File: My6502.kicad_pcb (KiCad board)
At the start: 2 copper layers, 99.7 x 99.7 mm, 28 parts, among them J1 IRQ_SEL, J2 CLK Jumper, J4 Expansion Port, J5 IRQ_Pullup, SW1 RESET, U1 ROM 28C256, U2 CPU 6502, U3 RAM 62256, U4 74HCT00, U5 74HCT02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

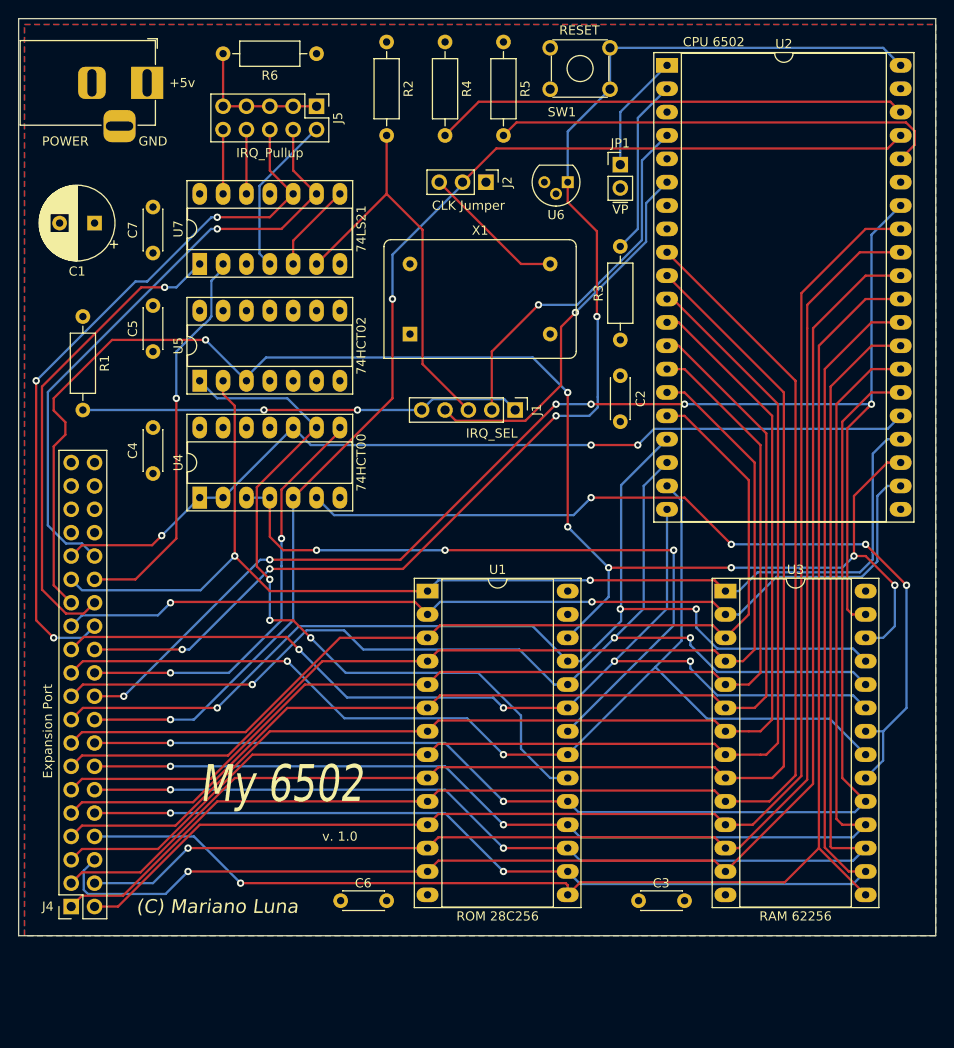
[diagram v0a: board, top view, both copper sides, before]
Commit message: Edge board completed and routed
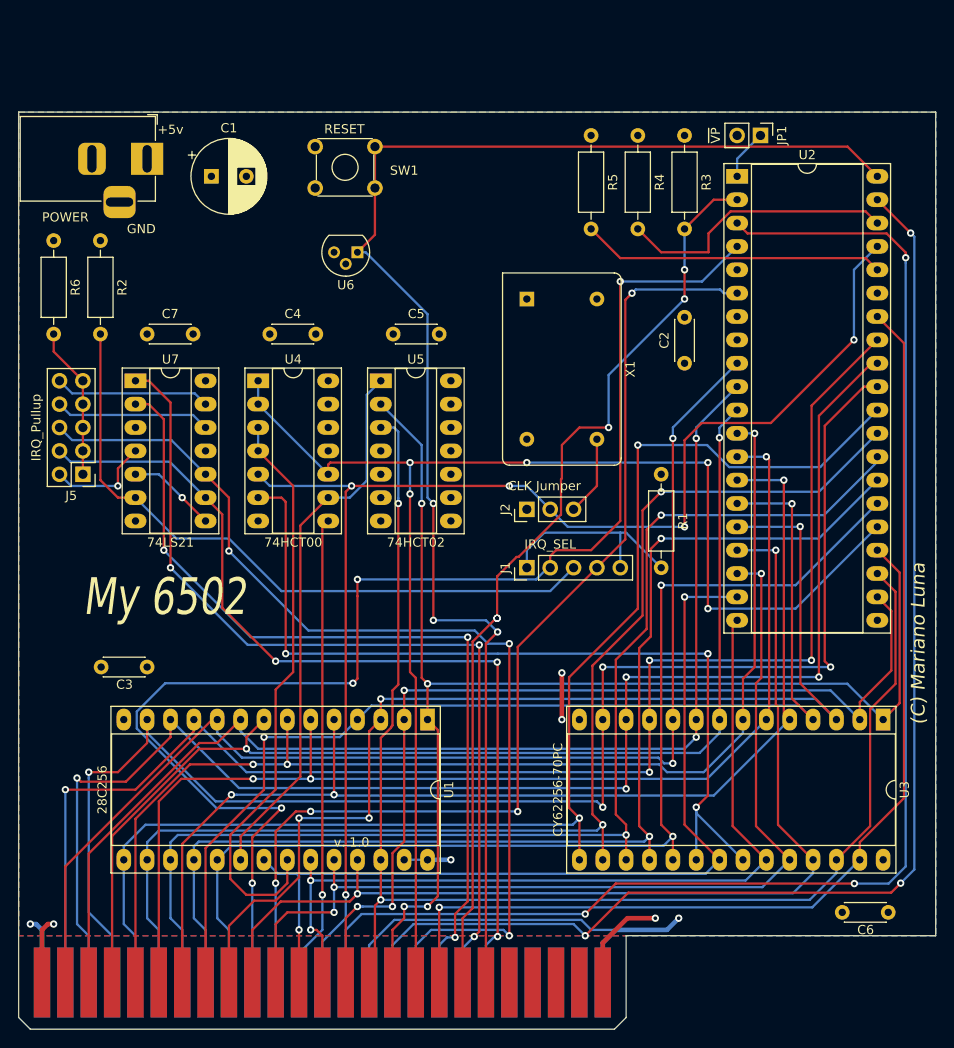
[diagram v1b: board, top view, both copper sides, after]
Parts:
- removed J4: Expansion Port, Connector_PinSocket_2.54mm:PinSocket_2x20_P2.54mm_Vertical
- added 6502_BUS1: 6502_BUS, A2_Slot_Footorint:BUS_A2, F.Cu at (56.5, 154.9)
- U1: value ROM 28C256 -> 28C256
- U2: value CPU 6502 -> WD65C02; footprint Package_DIP:DIP-40_W25.4mm_Socket_LongPads -> Package_DIP:DIP-40_W15.24mm_Socket_LongPads
- U3: value RAM 62256 -> CY62256-70PC
- moved R1 65.2 mm to (101.0, 99.7)
- moved C6 59.5 mm to (125.7, 147.3), turned to 180 degrees
- moved C3 59.2 mm to (45.1, 120.7), turned to 180 degrees
- moved J5 47.4 mm to (38.1, 99.7), turned to 180 degrees
- moved R2 37.9 mm to (40.0, 74.3)
- moved J2 35.8 mm to (86.4, 103.5), turned to 90 degrees
- moved R6 35.1 mm to (34.9, 74.3), turned to 270 degrees
- moved SW1 27.7 mm to (63.4, 64.1)
- moved C5 26.2 mm to (71.8, 84.5), turned to 0 degrees
- moved U6 24.1 mm to (67.9, 75.6)
- moved R3 23.3 mm to (103.5, 62.9), turned to 270 degrees
- moved R4 23.3 mm to (98.4, 62.9)
- moved U3 22.1 mm to (125.1, 126.4), turned to 270 degrees
- moved C4 19.8 mm to (58.4, 84.5), turned to 0 degrees
- moved U5 19.7 mm to (70.5, 89.5), turned to 0 degrees
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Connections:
- net Net-(J1-Pad4) renamed ~NMI
- net Net-(R3-Pad2) renamed RDY
- J1 pad 2: Net-(J1-Pad2) -> ~IRQ
- J1 pad 3: ~IRQ -> ~IRQ_TO_CPU
- R2 pad 2: ~IRQ -> ~IRQ_TO_CPU
- U2 pad 3: Net-(U2-Pad3) -> PHI_1
- U2 pad 39: Net-(U2-Pad39) -> PHI_2
- U2 pad 4: Net-(J1-Pad2) -> ~IRQ
- U7 pad 6: ~IRQ -> ~IRQ_TO_CPU
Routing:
- net PHI_1: track 0.00 -> 155.8 mm, vias 0 -> 3
- net PHI_2: track 0.00 -> 139.7 mm, vias 0 -> 3
- net ~IRQ: track 44.3 -> 149.9 mm, vias 0 -> 5
- net RDY: track 19.2 -> 101.0 mm, vias 0 -> 5
- net ~NMI: track 41.7 -> 116.9 mm, vias 1 -> 4
- net ~IRQ_TO_CPU: track 0.00 -> 73.4 mm
- net GND: track 0.00 -> 58.5 mm, vias 0 -> 4
- net a15: track 98.1 -> 150.5 mm, vias 3 -> 5
- net ~VIA2_IRQ: track 42.7 -> 94.3 mm, vias 1 -> 3
- net ~VIA1_IRQ: track 52.0 -> 97.2 mm, vias 1 -> 3
- net Net-(J1-Pad2): track 40.2 -> 0.00 mm, vias 1 -> 0
- net ~ACIA_IRQ: track 67.1 -> 101.6 mm, vias 1 -> 3
- net EXP_IRQ: track 78.1 -> 108.9 mm
- net R~W: track 146.1 -> 118.3 mm, vias 6 -> 1
- net Net-(J1-Pad1): track 48.0 -> 22.7 mm, vias 2 -> 0
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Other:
- outline, holes or cut-outs redrawn

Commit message: moving to a backplane
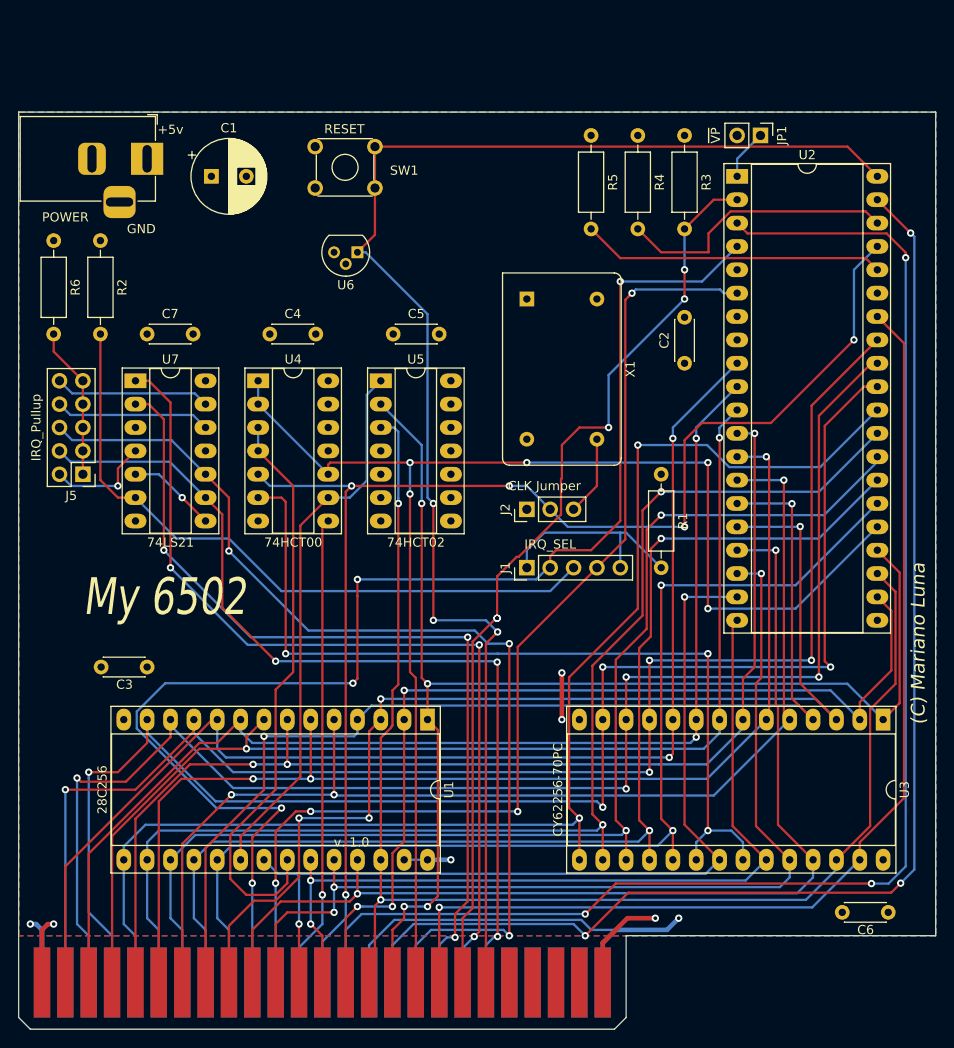
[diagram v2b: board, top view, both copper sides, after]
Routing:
- net ~RAM_CS: track 96.3 -> 94.8 mm
- net a9: track 105.2 -> 106.3 mm
- net a3: track 128.3 -> 127.2 mm
- net d5: track 132.0 -> 131.1 mm
- net a6: track 124.2 -> 125.1 mm
- net d0: track 158.3 -> 159.1 mm
- net d6: track 127.8 -> 127.2 mm
- net a1: track 128.6 -> 128.1 mm

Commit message: PCB completed CPU Board no clock
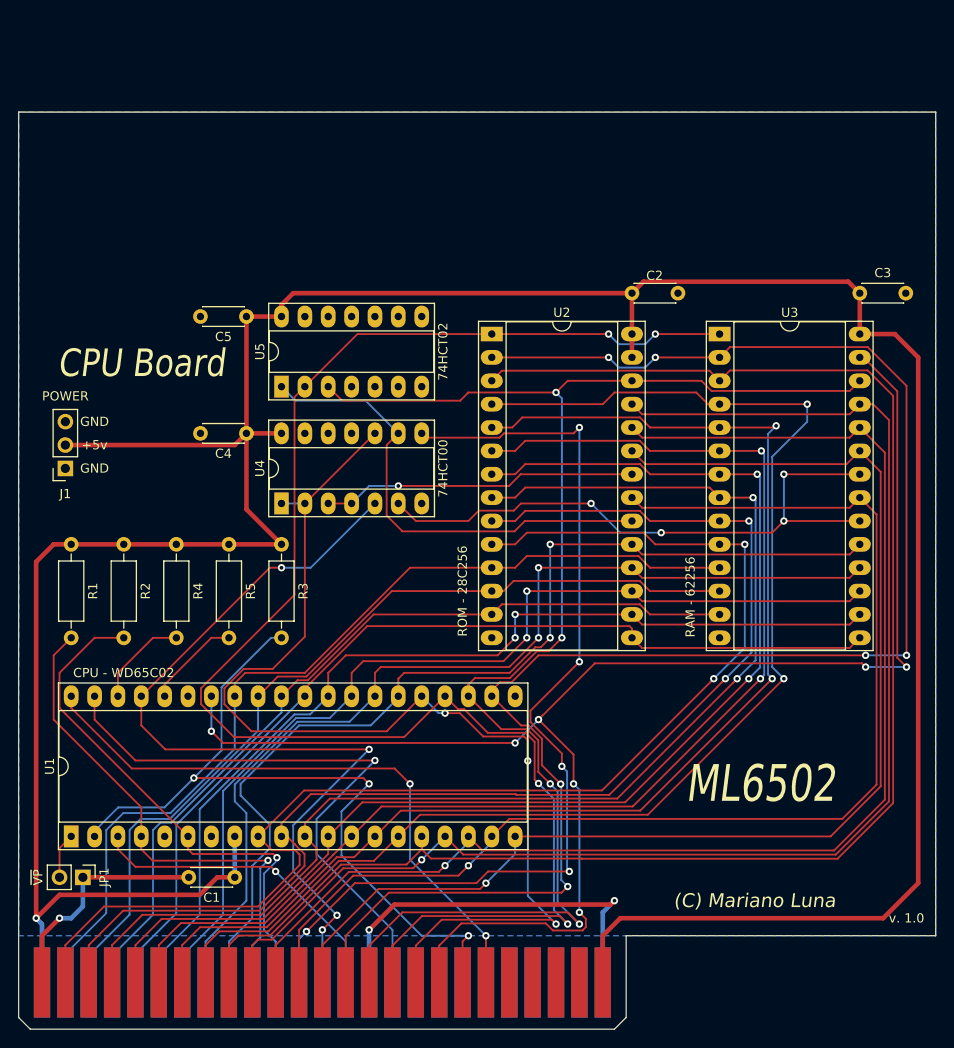
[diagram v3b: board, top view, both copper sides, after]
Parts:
- removed the C1 at (52.1, 67.3)
- removed the C3 at (45.1, 120.7)
- removed C6, C7: 0.1uF, Capacitor_THT:C_Disc_D4.3mm_W1.9mm_P5.00mm
- removed J2: CLK Jumper, Connector_PinHeader_2.54mm:PinHeader_1x03_P2.54mm_Vertical
- removed J5: IRQ_Pullup, Connector_PinHeader_2.54mm:PinHeader_2x05_P2.54mm_Vertical
- removed POWER: Barrel_Jack_Switch, Connector_BarrelJack:BarrelJack_Horizontal
- removed R6: 4K7, Resistor_THT:R_Axial_DIN0207_L6.3mm_D2.5mm_P10.16mm_Horizontal
- removed SW1: RESET, Button_Switch_THT:SW_TH_Tactile_Omron_B3F-10xx
- removed U6: DS1813-10, Package_TO_SOT_THT:TO-92
- removed U7: 74LS21, Package_DIP:DIP-14_W7.62mm_Socket_LongPads
- removed X1: CXO_DIP14, Oscillator:Oscillator_DIP-14
- added C2: 0.1uF, Capacitor_THT:C_Disc_D4.3mm_W1.9mm_P5.00mm, F.Cu at (97.8, 80.0)
- added C4: 0.1uF, Capacitor_THT:C_Disc_D4.3mm_W1.9mm_P5.00mm, F.Cu at (55.9, 95.2)
- J1: value IRQ_SEL -> POWER; footprint Connector_PinHeader_2.54mm:PinHeader_1x05_P2.54mm_Vertical -> Connector_PinSocket_2.54mm:PinSocket_1x03_P2.54mm_Vertical
- R1, R2, R3, R4, R5: value 4K7 -> 3K3
- U1: value 28C256 -> CPU - WD65C02; footprint Package_DIP:DIP-28_W15.24mm_Socket_LongPads -> Package_DIP:DIP-40_W15.24mm_Socket_LongPads
- U2: value WD65C02 -> ROM - 28C256; footprint Package_DIP:DIP-40_W15.24mm_Socket_LongPads -> Package_DIP:DIP-28_W15.24mm_Socket_LongPads
- U3: value CY62256-70PC -> RAM - 62256
- moved JP1 109.2 mm to (38.1, 143.5)
- moved C1 74.3 mm to (54.6, 143.5), turned to 180 degrees
- moved R4 67.0 mm to (48.3, 107.3)
- moved R1 64.6 mm to (36.8, 107.3)
- moved C3 64.3 mm to (122.6, 80.0)
- moved R3 62.4 mm to (59.7, 107.3)
- moved R5 59.4 mm to (54.0, 107.3)
- moved J1 51.3 mm to (36.2, 99.1), turned to 180 degrees
- moved U3 45.5 mm to (107.3, 84.5), turned to 0 degrees
- moved U1 40.8 mm to (36.8, 139.1), turned to 90 degrees
- moved R2 33.1 mm to (42.5, 107.3)
- moved U2 31.7 mm to (82.5, 84.5)
- moved C5 16.1 mm to (55.9, 82.5), turned to 180 degrees
- moved U4 13.6 mm to (59.7, 102.9), turned to 90 degrees
- moved U5 10.8 mm to (59.7, 90.2), turned to 90 degrees
- renumbered C2 to C1, C4 to C3
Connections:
- J1 pad 1: Net-(J1-Pad1) -> GND
- J1 pad 2: ~IRQ -> +5V
- J1 pad 3: ~IRQ_TO_CPU -> GND
- JP1 pad 1: Net-(JP1-Pad1) -> GND
- JP1 pad 2: +5V -> Net-(JP1-Pad2)
- R1 pad 2: Net-(J1-Pad1) -> ~IRQ
- R2 pad 2: ~IRQ_TO_CPU -> ~NMI
- U1 pad 1: a14 -> Net-(JP1-Pad2)
- U1 pad 10: a0 -> a1
- U1 pad 11: d0 -> a2
- U1 pad 12: d1 -> a3
- U1 pad 13: d2 -> a4
- U1 pad 14: GND -> a5
- U1 pad 15: d3 -> a6
- U1 pad 16: d4 -> a7
- U1 pad 17: d5 -> a8
- U1 pad 18: d6 -> a9
- U1 pad 19: d7 -> a10
- U1 pad 2: a12 -> RDY
- U1 pad 20: ~ROM_CS -> a11
- U1 pad 21: a10 -> GND
- U1 pad 22: ~ROM_OE -> a12
- U1 pad 23: a11 -> a13
- U1 pad 24: a9 -> a14
- U1 pad 25: a8 -> a15
- U1 pad 26: a13 -> d7
- U1 pad 27: +5V -> d6
- U1 pad 28: +5V -> d5
- U1 pad 3: a7 -> PHI_1
- U1 pad 4: a6 -> ~IRQ
- U1 pad 5: a5 -> Net-(U1-Pad5)
- U1 pad 6: a4 -> ~NMI
- U1 pad 7: a3 -> Net-(U1-Pad7)
- U1 pad 8: a2 -> +5V
- U1 pad 9: a1 -> a0
- U2 pad 1: Net-(JP1-Pad1) -> a14
- U2 pad 10: a1 -> a0
- U2 pad 11: a2 -> d0
- U2 pad 12: a3 -> d1
- U2 pad 13: a4 -> d2
- U2 pad 14: a5 -> GND
- U2 pad 15: a6 -> d3
- U2 pad 16: a7 -> d4
- U2 pad 17: a8 -> d5
- U2 pad 18: a9 -> d6
- U2 pad 19: a10 -> d7
- U2 pad 2: RDY -> a12
- U2 pad 20: a11 -> ~ROM_CS
- U2 pad 21: GND -> a10
- U2 pad 22: a12 -> ~ROM_OE
- U2 pad 23: a13 -> a11
- U2 pad 24: a14 -> a9
- U2 pad 25: a15 -> a8
- U2 pad 26: d7 -> a13
- U2 pad 27: d6 -> +5V
- U2 pad 28: d5 -> +5V
- U2 pad 3: PHI_1 -> a7
- U2 pad 4: ~IRQ -> a6
- U2 pad 5: Net-(U2-Pad5) -> a5
- U2 pad 6: ~NMI -> a4
- U2 pad 7: Net-(U2-Pad7) -> a3
- U2 pad 8: +5V -> a2
- U2 pad 9: a0 -> a1
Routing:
- net +5V: track 23.5 -> 338.9 mm, vias 3 -> 1
- net PHI_1: track 155.8 -> 34.8 mm, vias 3 -> 1
- net EXP_IRQ: track 108.9 -> 0.00 mm, vias 3 -> 0
- net ~ACIA_IRQ: track 101.6 -> 0.00 mm, vias 3 -> 0
- net ~VIA1_IRQ: track 97.2 -> 0.00 mm, vias 3 -> 0
- net ~VIA2_IRQ: track 94.3 -> 0.00 mm, vias 3 -> 0
- net ~IRQ: track 149.9 -> 56.0 mm, vias 5 -> 1
- net ~RESET: track 158.3 -> 66.5 mm, vias 3 -> 2
- net a12: track 102.8 -> 180.8 mm, vias 3 -> 6
- net PHI_2: track 139.7 -> 65.0 mm, vias 3 -> 1
- net ~IRQ_TO_CPU: track 73.4 -> 0.00 mm
- net d2: track 162.4 -> 91.7 mm, vias 4 -> 0
- net d1: track 160.2 -> 96.4 mm, vias 4 -> 0
- net ~NMI: track 116.9 -> 58.2 mm, vias 4 -> 1
- net d0: track 159.1 -> 102.1 mm, vias 4 -> 0
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- removed copper zone on F.Cu, net +5V
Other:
- board text added: "CPU Board"
- board text added: "ML6502"
- board text removed: "My 6502"

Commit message: Rev 1 with silkscreen
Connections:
- net EXP_IRQ renamed Net-(6502_BUS1-Pad34)
- net ~ACIA_IRQ renamed Net-(6502_BUS1-Pad31)
- net ~VIA1_IRQ renamed Net-(6502_BUS1-Pad32)
- net ~VIA2_IRQ renamed Net-(6502_BUS1-Pad33)
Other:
- board text added: "I/O 8k bytes $8000-$9FFF"
- board text added: "RAM 32k bytes $0000-$7FFF"
- board text added: "ROM 24k bytes $A000-$FFFF"
